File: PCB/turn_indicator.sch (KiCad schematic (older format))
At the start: 15 parts

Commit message: pcb subfolder and unknown pending changes
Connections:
- net CLOCK_LEDS_L renamed CLOCK_LEDS_F
- net CLOCK_LEDS_R renamed CLOCK_LEDS_B
- net DATA_LEDS_L renamed DATA_LEDS_F
- net DATA_LEDS_R renamed DATA_LEDS_B
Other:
- note added: "going from left high to right high"
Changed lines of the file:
@@
 PWR_IND
 Text GLabel 3950 3800 2    50   Input ~ 0
-DATA_LEDS_L
+DATA_LEDS_F
 Text GLabel 3950 3900 2    50   Input ~ 0
-CLOCK_LEDS_L
+CLOCK_LEDS_F
 $Comp
 L Connector:Conn_01x02_Male J_LIPO_SW_M1
@@
 $EndComp
 Text GLabel 4900 6850 0    50   Input ~ 0
-DATA_LEDS_R
+DATA_LEDS_B
 Text GLabel 4900 6750 0    50   Input ~ 0
-CLOCK_LEDS_R
+CLOCK_LEDS_B
 Wire Wire Line
 	4900 6500 4900 6650
 Text GLabel 4900 6350 0    50   Input ~ 0
-DATA_LEDS_L
+DATA_LEDS_F
 Text GLabel 4900 6250 0    50   Input ~ 0
-CLOCK_LEDS_L
+CLOCK_LEDS_F
 Wire Wire Line
 	4200 6000 4900 6000
@@
 $EndComp
 Text GLabel 3950 4000 2    50   Input ~ 0
-DATA_LEDS_R
+DATA_LEDS_B
 Text GLabel 3950 4100 2    50   Input ~ 0
-CLOCK_LEDS_R
+CLOCK_LEDS_B
 Wire Wire Line
 	5450 1350 5450 1450
@@
 Wire Wire Line
 	6850 1400 6850 1350
+Text Notes 5250 6050 0    50   ~ 0
+going from left high to right high
 $EndSCHEMATC

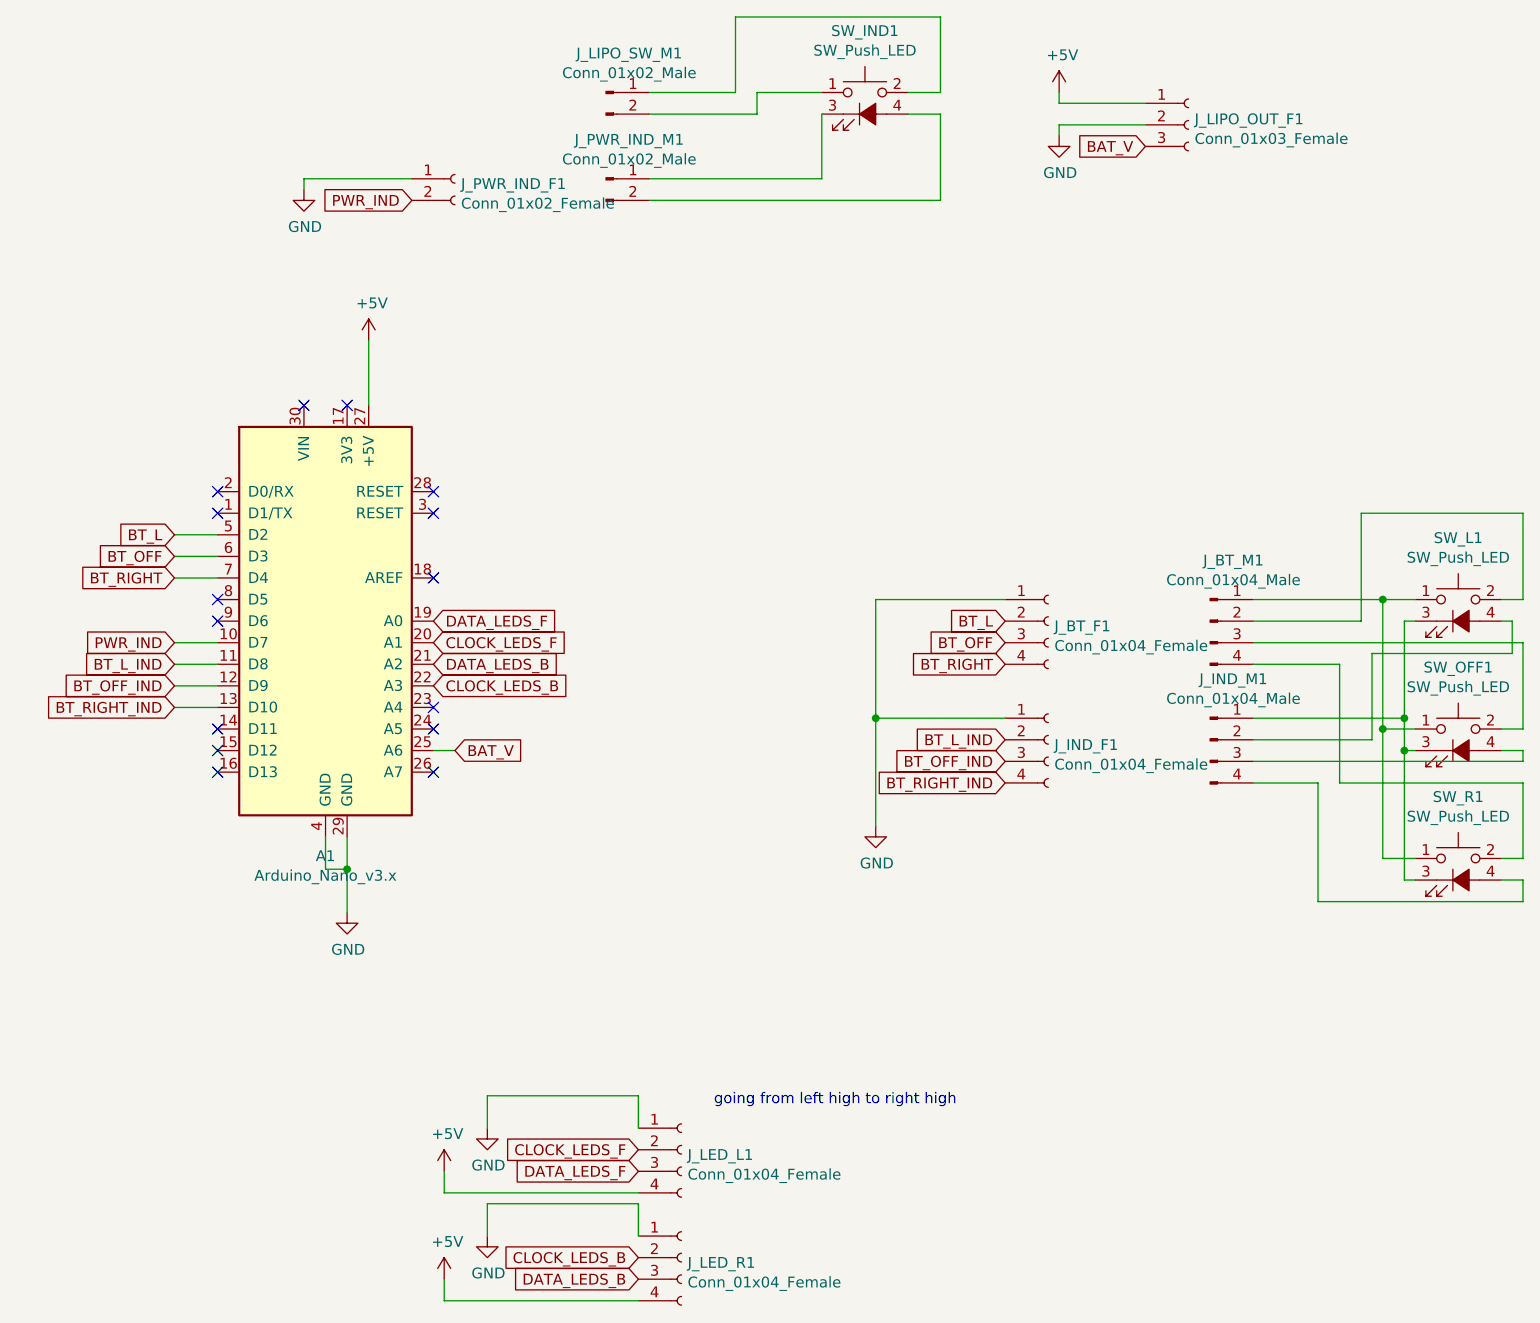
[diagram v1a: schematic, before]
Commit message: shrink to 5x7 perfboard, add comments, add fuse and capacitors
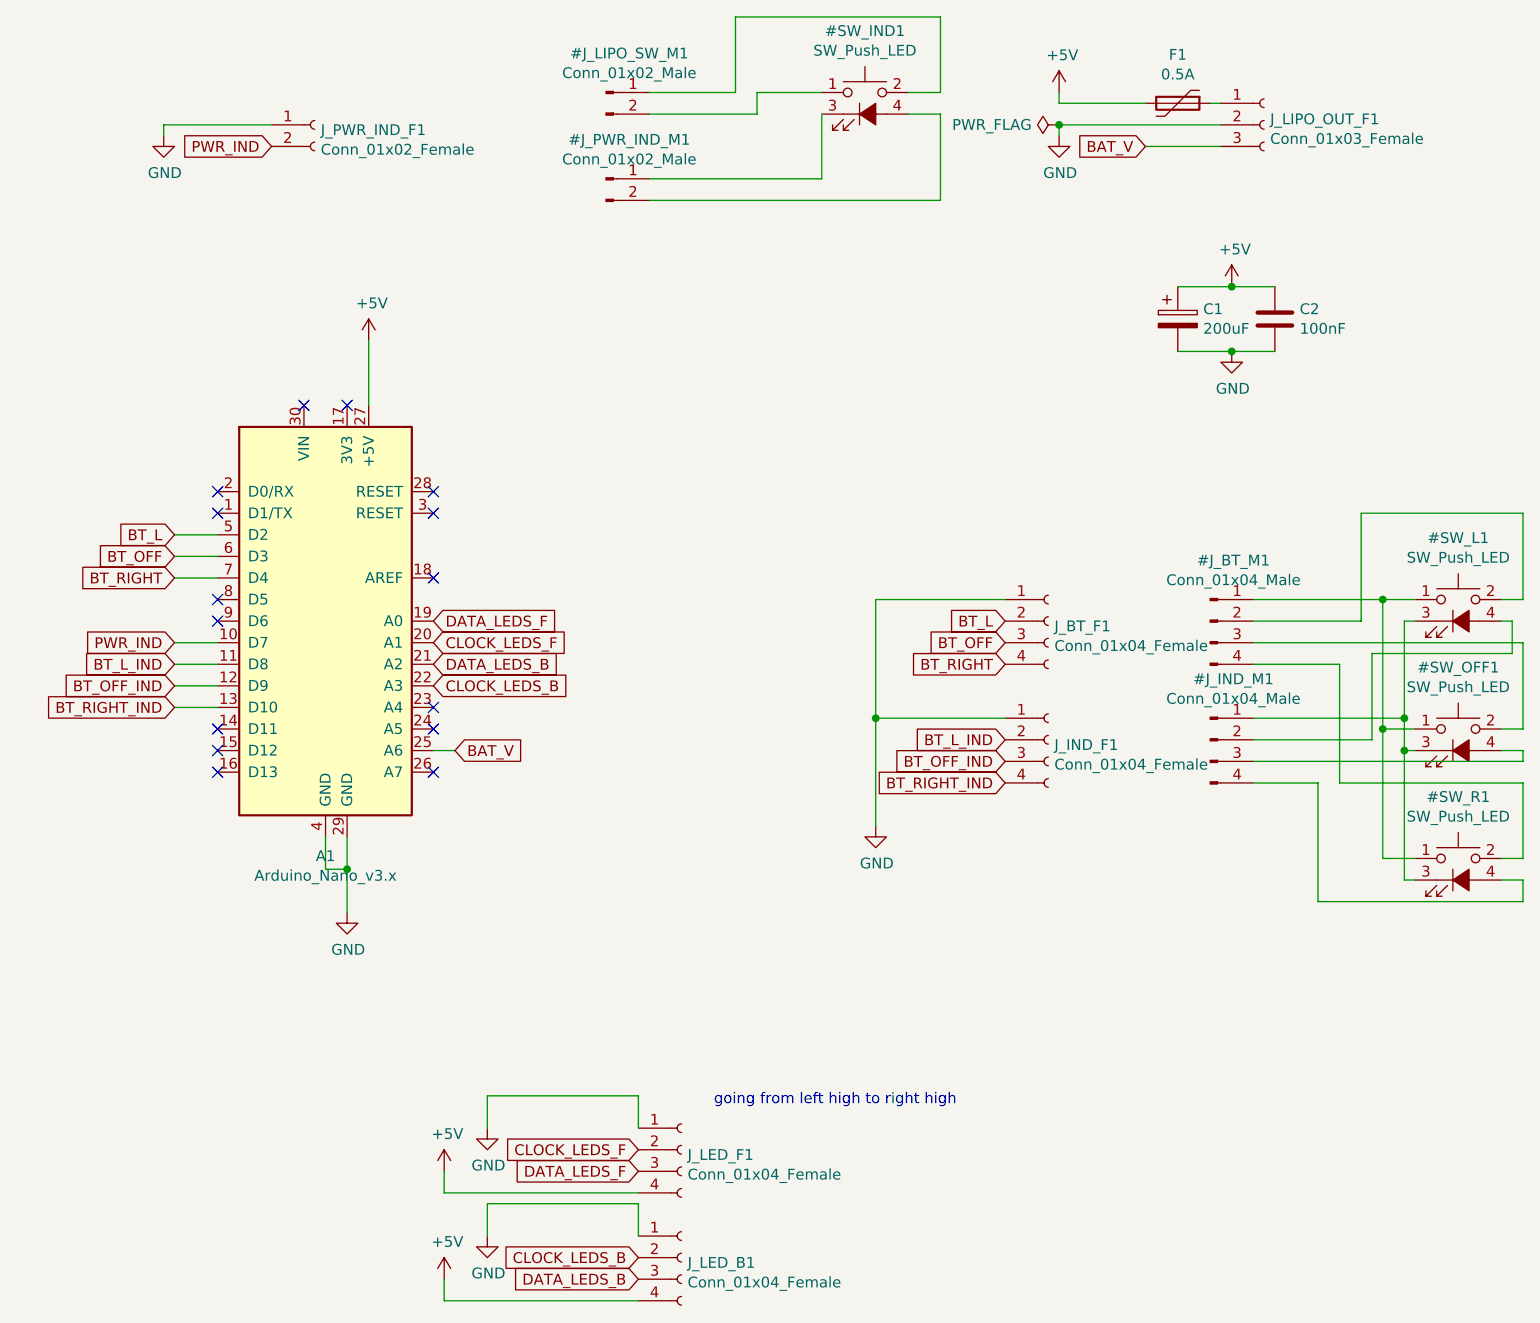
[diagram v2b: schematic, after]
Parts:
- removed J_BT_M1, J_IND_M1: Conn_01x04_Male, symbol Connector:Conn_01x04_Male
- removed J_LIPO_SW_M1, J_PWR_IND_M1: Conn_01x02_Male, symbol Connector:Conn_01x02_Male
- removed SW_IND1, SW_L1, SW_OFF1, SW_R1: SW_Push_LED, symbol Switch:SW_Push_LED
- added C1: 200uF, Capacitor_THT:CP_Radial_D8.0mm_P2.50mm, symbol Device:CP
- added C2: 100nF, Capacitor_SMD:C_0603_1608Metric, symbol Device:C
- added F1: 0.5A, Fuse:Fuse_0805_2012Metric, symbol Device:Polyfuse
- renumbered J_LED_R1 to J_LED_B1, J_LED_L1 to J_LED_F1
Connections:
- net +5V: now also C1.1, C2.1, F1.2; no longer J_LIPO_OUT_F1.1 (Pin_1)
- net GND: now also C1.2, C2.2
- new net: F1.1, J_LIPO_OUT_F1.1 (Pin_1)
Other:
- moved on the sheet: J_LIPO_OUT_F1, J_PWR_IND_F1
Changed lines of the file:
@@
 $EndComp
 $Comp
-L Switch:SW_Push_LED SW_L1
+L Switch:SW_Push_LED #SW_L1
 U 1 1 6000913A
 P 8700 3800
-F 0 "SW_L1" H 8700 4185 50  0000 C CNN
+F 0 "#SW_L1" H 8700 4185 50  0000 C CNN
 F 1 "SW_Push_LED" H 8700 4094 50  0000 C CNN
 F 2 "" H 8700 4100 50  0001 C CNN
@@
 $EndComp
 $Comp
-L Switch:SW_Push_LED SW_OFF1
+L Switch:SW_Push_LED #SW_OFF1
 U 1 1 6000A0A3
 P 8700 4400
-F 0 "SW_OFF1" H 8700 4785 50  0000 C CNN
+F 0 "#SW_OFF1" H 8700 4785 50  0000 C CNN
 F 1 "SW_Push_LED" H 8700 4694 50  0000 C CNN
 F 2 "" H 8700 4700 50  0001 C CNN
@@
 $EndComp
 $Comp
-L Switch:SW_Push_LED SW_R1
+L Switch:SW_Push_LED #SW_R1
 U 1 1 6000A32F
 P 8700 5000
-F 0 "SW_R1" H 8700 5385 50  0000 C CNN
+F 0 "#SW_R1" H 8700 5385 50  0000 C CNN
 F 1 "SW_Push_LED" H 8700 5294 50  0000 C CNN
 F 2 "" H 8700 5300 50  0001 C CNN
@@
 Connection ~ 8450 4400
 $Comp
-L Connector:Conn_01x04_Male J_BT_M1
+L Connector:Conn_01x04_Male #J_BT_M1
 U 1 1 6004EA5E
 P 7550 3800
-F 0 "J_BT_M1" H 7658 4081 50  0000 C CNN
+F 0 "#J_BT_M1" H 7658 4081 50  0000 C CNN
 F 1 "Conn_01x04_Male" H 7658 3990 50  0000 C CNN
 F 2 "" H 7550 3800 50  0001 C CNN
@@
 $EndComp
 $Comp
-L Connector:Conn_01x04_Male J_IND_M1
+L Connector:Conn_01x04_Male #J_IND_M1
 U 1 1 6004F854
 P 7550 4350
-F 0 "J_IND_M1" H 7658 4631 50  0000 C CNN
+F 0 "#J_IND_M1" H 7658 4631 50  0000 C CNN
 F 1 "Conn_01x04_Male" H 7658 4540 50  0000 C CNN
 F 2 "" H 7550 4350 50  0001 C CNN
@@
 CLOCK_LEDS_F
 $Comp
-L Connector:Conn_01x02_Male J_LIPO_SW_M1
+L Connector:Conn_01x02_Male #J_LIPO_SW_M1
 U 1 1 6005A1E3
 P 4750 1350
-F 0 "J_LIPO_SW_M1" H 4858 1531 50  0000 C CNN
+F 0 "#J_LIPO_SW_M1" H 4858 1531 50  0000 C CNN
 F 1 "Conn_01x02_Male" H 4858 1440 50  0000 C CNN
 F 2 "" H 4750 1350 50  0001 C CNN
@@
 $EndComp
 $Comp
-L Connector:Conn_01x04_Female J_LED_L1
+L Connector:Conn_01x04_Female J_LED_F1
 U 1 1 6007A3E8
 P 5100 6250
-F 0 "J_LED_L1" H 5128 6226 50  0000 L CNN
+F 0 "J_LED_F1" H 5128 6226 50  0000 L CNN
 F 1 "Conn_01x04_Female" H 5128 6135 50  0000 L CNN
 F 2 "Connector_JST:JST_XH_B4B-XH-A_1x04_P2.50mm_Vertical" H 5100 6250 50  0001 C CNN
@@
 	4900 6000 4900 6150
 $Comp
-L Connector:Conn_01x04_Female J_LED_R1
+L Connector:Conn_01x04_Female J_LED_B1
 U 1 1 600A0FBA
 P 5100 6750
-F 0 "J_LED_R1" H 5128 6726 50  0000 L CNN
+F 0 "J_LED_B1" H 5128 6726 50  0000 L CNN
 F 1 "Conn_01x04_Female" H 5128 6635 50  0000 L CNN
 F 2 "Connector_JST:JST_XH_B4B-XH-A_1x04_P2.50mm_Vertical" H 5100 6750 50  0001 C CNN
@@
 $EndComp
 $Comp
-L Switch:SW_Push_LED SW_IND1
+L Switch:SW_Push_LED #SW_IND1
 U 1 1 60022BB2
 P 5950 1450
-F 0 "SW_IND1" H 5950 1835 50  0000 C CNN
+F 0 "#SW_IND1" H 5950 1835 50  0000 C CNN
 F 1 "SW_Push_LED" H 5950 1744 50  0000 C CNN
 F 2 "" H 5950 1750 50  0001 C CNN
@@
 Wire Wire Line
 	5750 1450 5750 1750
-Text GLabel 3850 1850 0    50   Input ~ 0
+Text GLabel 3200 1600 0    50   Input ~ 0
 PWR_IND
 NoConn ~ 3950 3200
@@
 Connection ~ 3550 4950
 $Comp
-L Connector:Conn_01x02_Male J_PWR_IND_M1
+L Connector:Conn_01x02_Male #J_PWR_IND_M1
 U 1 1 6010B895
 P 4750 1750
-F 0 "J_PWR_IND_M1" H 4858 1931 50  0000 C CNN
+F 0 "#J_PWR_IND_M1" H 4858 1931 50  0000 C CNN
 F 1 "Conn_01x02_Male" H 4858 1840 50  0000 C CNN
 F 2 "" H 4750 1750 50  0001 C CNN
@@
 L Connector:Conn_01x03_Female J_LIPO_OUT_F1
 U 1 1 6010F68E
-P 7450 1500
-F 0 "J_LIPO_OUT_F1" H 7478 1526 50  0000 L CNN
-F 1 "Conn_01x03_Female" H 7478 1435 50  0000 L CNN
-F 2 "Connector_JST:JST_XH_B3B-XH-A_1x03_P2.50mm_Vertical" H 7450 1500 50  0001 C CNN
-F 3 "~" H 7450 1500 50  0001 C CNN
-	1    7450 1500
+P 7800 1500
+F 0 "J_LIPO_OUT_F1" H 7828 1526 50  0000 L CNN
+F 1 "Conn_01x03_Female" H 7828 1435 50  0000 L CNN
+F 2 "Connector_JST:JST_XH_B3B-XH-A_1x03_P2.50mm_Vertical" H 7800 1500 50  0001 C CNN
+F 3 "~" H 7800 1500 50  0001 C CNN
+	1    7800 1500
 	1    0    0    -1
 $EndComp
@@
 L Connector:Conn_01x02_Female J_PWR_IND_F1
 U 1 1 6011230A
-P 4050 1750
-F 0 "J_PWR_IND_F1" H 4078 1726 50  0000 L CNN
-F 1 "Conn_01x02_Female" H 4078 1635 50  0000 L CNN
-F 2 "Connector_JST:JST_XH_B2B-XH-A_1x02_P2.50mm_Vertical" H 4050 1750 50  0001 C CNN
-F 3 "~" H 4050 1750 50  0001 C CNN
-	1    4050 1750
+P 3400 1500
+F 0 "J_PWR_IND_F1" H 3428 1476 50  0000 L CNN
+F 1 "Conn_01x02_Female" H 3428 1385 50  0000 L CNN
+F 2 "Connector_JST:JST_XH_B2B-XH-A_1x02_P2.50mm_Vertical" H 3400 1500 50  0001 C CNN
+F 3 "~" H 3400 1500 50  0001 C CNN
+	1    3400 1500
 	1    0    0    -1
 $EndComp
@@
 L power:GND #PWR0110
 U 1 1 6013745F
-P 3350 1800
-F 0 "#PWR0110" H 3350 1550 50  0001 C CNN
-F 1 "GND" H 3355 1627 50  0000 C CNN
-F 2 "" H 3350 1800 50  0001 C CNN
-F 3 "" H 3350 1800 50  0001 C CNN
-	1    3350 1800
-	1    0    0    -1
-$EndComp
-Wire Wire Line
-	3850 1750 3350 1750
-Wire Wire Line
-	3350 1750 3350 1800
-Wire Wire Line
-	7250 1500 6850 1500
+P 2700 1550
+F 0 "#PWR0110" H 2700 1300 50  0001 C CNN
+F 1 "GND" H 2705 1377 50  0000 C CNN
+F 2 "" H 2700 1550 50  0001 C CNN
+F 3 "" H 2700 1550 50  0001 C CNN
+	1    2700 1550
+	1    0    0    -1
+$EndComp
+Wire Wire Line
+	3200 1500 2700 1500
+Wire Wire Line
+	2700 1500 2700 1550
 Wire Wire Line
 	6850 1500 6850 1550
@@
 Text Notes 5250 6050 0    50   ~ 0
 going from left high to right high
+$Comp
+L power:PWR_FLAG #FLG0101
+U 1 1 61146A23
+P 6850 1500
+F 0 "#FLG0101" H 6850 1575 50  0001 C CNN
+F 1 "PWR_FLAG" V 6850 1627 50  0000 L CNN
+F 2 "" H 6850 1500 50  0001 C CNN
+F 3 "~" H 6850 1500 50  0001 C CNN
+	1    6850 1500
+	0    -1   -1   0
+$EndComp
+Connection ~ 6850 1500
+$Comp
+L Device:CP C1
+U 1 1 61163E5D
+P 7400 2400
+F 0 "C1" H 7518 2446 50  0000 L CNN
+F 1 "200uF" H 7518 2355 50  0000 L CNN
+F 2 "Capacitor_THT:CP_Radial_D8.0mm_P2.50mm" H 7438 2250 50  0001 C CNN
+F 3 "~" H 7400 2400 50  0001 C CNN
+	1    7400 2400
+	1    0    0    -1
+$EndComp
+$Comp
+L Device:C C2
+U 1 1 6116454D
+P 7850 2400
+F 0 "C2" H 7965 2446 50  0000 L CNN
+F 1 "100nF" H 7965 2355 50  0000 L CNN
+F 2 "Capacitor_SMD:C_0603_1608Metric" H 7888 2250 50  0001 C CNN
+F 3 "~" H 7850 2400 50  0001 C CNN
+	1    7850 2400
+	1    0    0    -1
+$EndComp
+$Comp
+L power:GND #PWR0111
+U 1 1 611658AE
+P 7650 2550
+F 0 "#PWR0111" H 7650 2300 50  0001 C CNN
+F 1 "GND" H 7655 2377 50  0000 C CNN
+F 2 "" H 7650 2550 50  0001 C CNN
+F 3 "" H 7650 2550 50  0001 C CNN
+	1    7650 2550
+	1    0    0    -1
+$EndComp
+$Comp
+L power:+5V #PWR0112
+U 1 1 6116655D
+P 7650 2250
+F 0 "#PWR0112" H 7650 2100 50  0001 C CNN
+F 1 "+5V" H 7665 2423 50  0000 C CNN
+F 2 "" H 7650 2250 50  0001 C CNN
+F 3 "" H 7650 2250 50  0001 C CNN
+	1    7650 2250
+	1    0    0    -1
+$EndComp
+Wire Wire Line
+	7400 2250 7650 2250
+Connection ~ 7650 2250
+Wire Wire Line
+	7650 2250 7850 2250
+Wire Wire Line
+	7850 2550 7650 2550
+Connection ~ 7650 2550
+Wire Wire Line
+	7650 2550 7400 2550
+$Comp
+L Device:Polyfuse F1
+U 1 1 61175425
+P 7400 1400
+F 0 "F1" V 7175 1400 50  0000 C CNN
+F 1 "0.5A" V 7266 1400 50  0000 C CNN
+F 2 "Fuse:Fuse_0805_2012Metric" H 7450 1200 50  0001 L CNN
+F 3 "~" H 7400 1400 50  0001 C CNN
+	1    7400 1400
+	0    1    1    0
+$EndComp
+Wire Wire Line
+	7600 1400 7550 1400
+Wire Wire Line
+	6850 1500 7600 1500
+Wire Wire Line
+	7600 1600 7250 1600
 $EndSCHEMATC
